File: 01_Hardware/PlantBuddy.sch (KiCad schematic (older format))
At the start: 41 parts, among them J1 SWD+DBG, J2 Conn_I2C_SDA, J3 Conn_I2C_SCL, Q1 AO3401, Q2 AO3400A, U1 OPT3001, U2 nRF52810-QCxx, U3 LMC555xM, U6 SHTC3, Y1 32MHz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

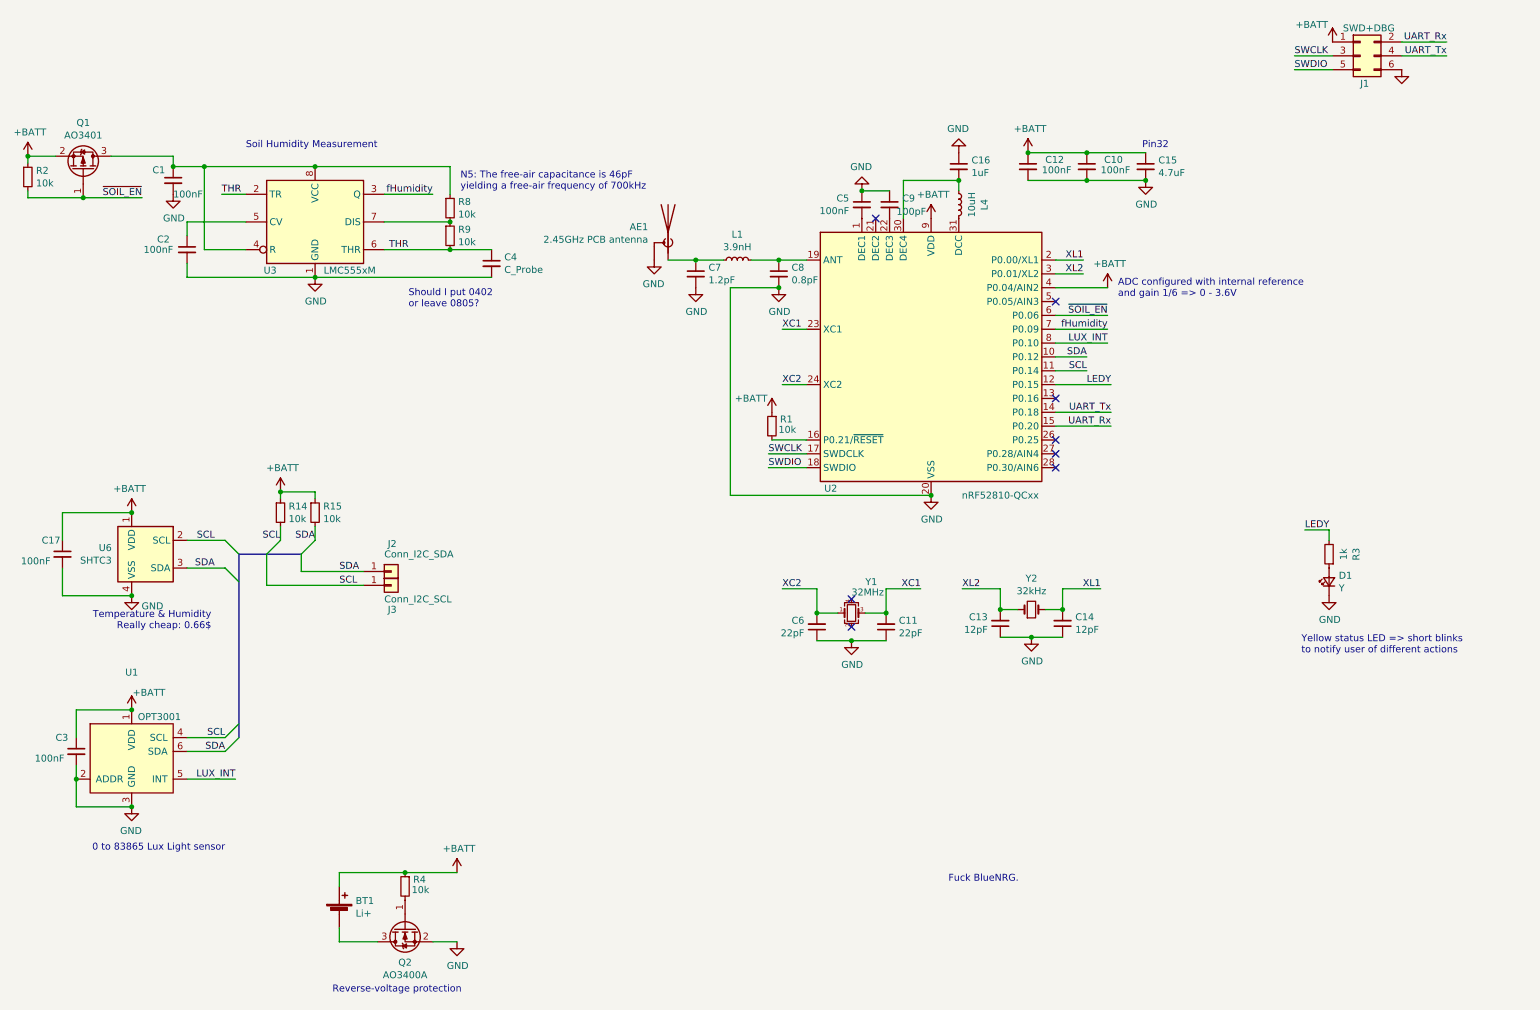
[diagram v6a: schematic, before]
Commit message: PlantBuddy Revision 3. Switched to nRF52832
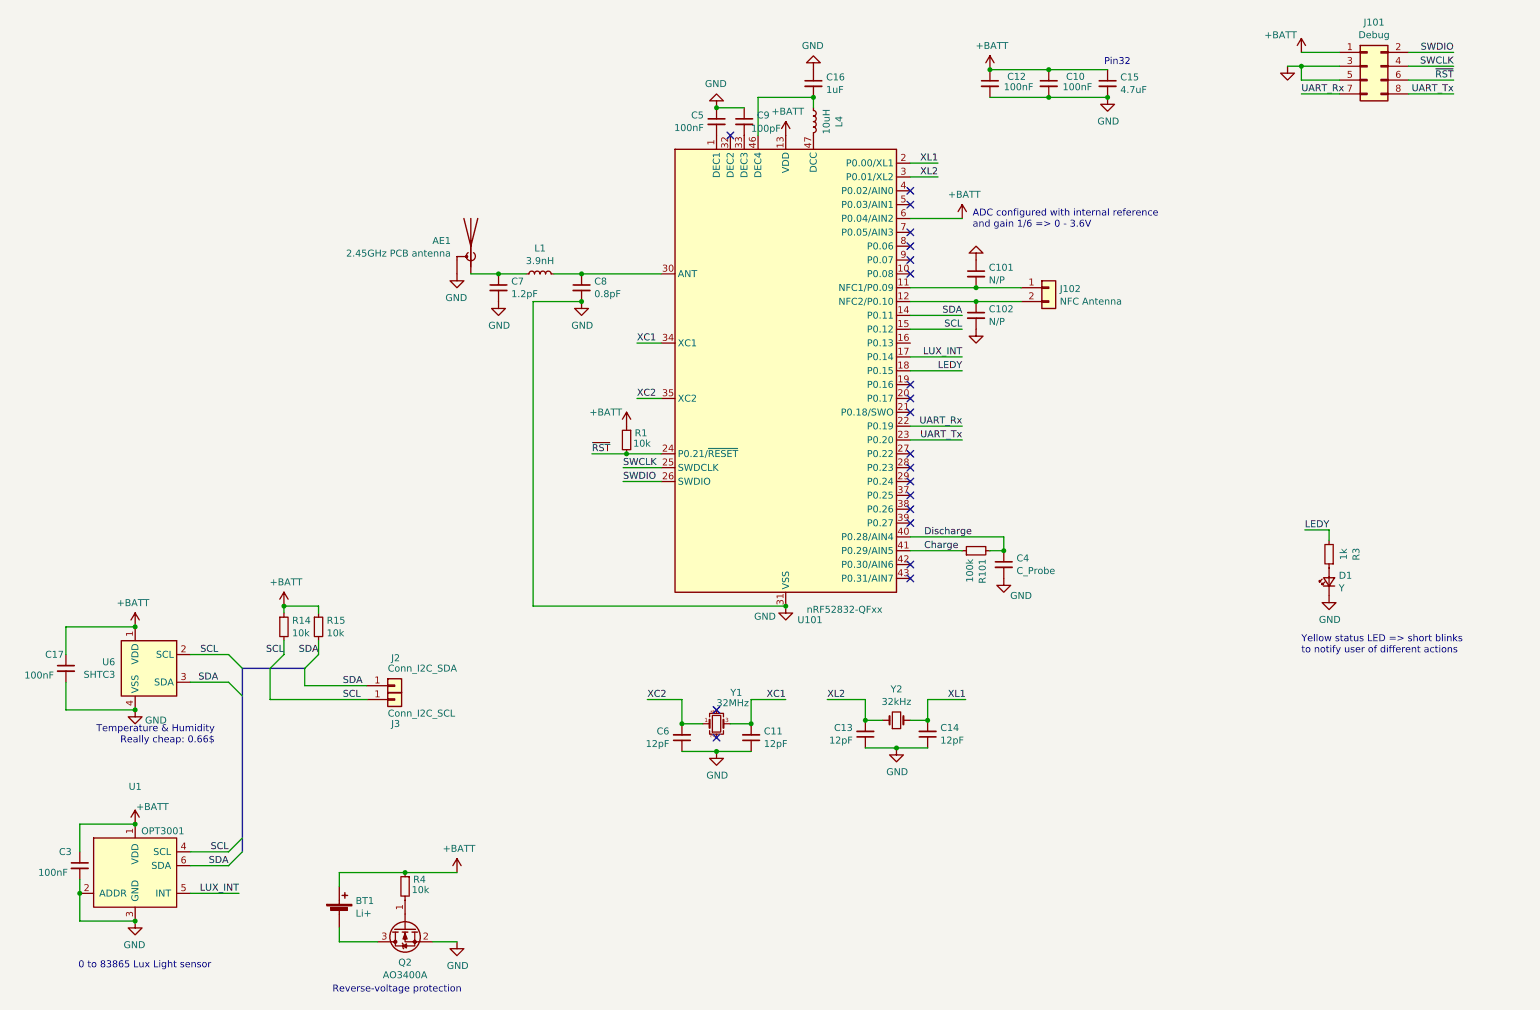
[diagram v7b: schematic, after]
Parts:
- removed C1, C2: 100nF, Capacitor_SMD:C_0402_1005Metric, symbol PlantBuddy-rescue:C_Small-Device
- removed J1: SWD+DBG, Connector_PinHeader_2.54mm:PinHeader_2x03_P2.54mm_Vertical, symbol Connector_Generic:Conn_02x03_Odd_Even
- removed Q1: AO3401, Package_TO_SOT_SMD:SOT-23, symbol PlantBuddy-rescue:AO3401A-Transistor_FET
- removed R2, R8, R9: 10k, Resistor_SMD:R_0402_1005Metric, symbol PlantBuddy-rescue:R_Small-Device
- removed U2: nRF52810-QCxx, Package_DFN_QFN:QFN-32-1EP_5x5mm_P0.5mm_EP3.6x3.6mm_ThermalVias, symbol PlantBuddy-rescue:nRF52810-QCxx-MCU_Nordic
- removed U3: LMC555xM, Package_SO:SOIC-8_3.9x4.9mm_P1.27mm, symbol PlantBuddy-rescue:LMC555xM-Timer
- added C101, C102: N/P, Capacitor_SMD:C_0402_1005Metric, symbol PlantBuddy-rescue:C_Small-Device
- added J101: Debug, PlantBuddy:PinHeader_2x04_P1.27mm_Vertical, symbol Connector_Generic:Conn_02x04_Odd_Even
- added J102: NFC Antenna, Connector_PinHeader_2.54mm:PinHeader_1x02_P2.54mm_Vertical, symbol Connector_Generic:Conn_01x02
- added R101: 100k, Resistor_SMD:R_0402_1005Metric, symbol Device:R_Small
- added U101: nRF52832-QFxx, Package_DFN_QFN:QFN-48-1EP_6x6mm_P0.4mm_EP4.6x4.6mm_ThermalVias, symbol MCU_Nordic:nRF52832-QFxx
- C11, C6: value 22pF -> 12pF
- C8: LCSC C326068 -> C285068
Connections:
- net +BATT: now also J101.1 (Pin_1), U101.13 (VDD), U101.36 (VDD), U101.48 (VDD), U101.6 (P0.04/AIN2)
- net GND: now also C101.1, C102.2, J101.3 (Pin_3), J101.5 (Pin_5), U101.31 (VSS), U101.45 (VSS), U101.49 (VSS)
- net LEDY: now also U101.18 (P0.15)
- net LUX_INT: now also U101.17 (P0.14)
- net SCL: now also U101.15 (P0.12)
- net SDA: now also U101.14 (P0.11)
- net SWCLK: now also J101.4 (Pin_4), U101.25 (SWDCLK)
- net SWDIO: now also J101.2 (Pin_2), U101.26 (SWDIO)
- net UART_Rx: now also J101.7 (Pin_7), U101.22 (P0.19)
- net UART_Tx: now also J101.8 (Pin_8), U101.23 (P0.20)
- net XC1: now also U101.34 (XC1)
- net XC2: now also U101.35 (XC2)
- net XL1: now also U101.2 (P0.00/XL1)
- net XL2: now also U101.3 (P0.01/XL2)
- net at C16.2, L4.1: now also U101.46 (DEC4)
- net at L4.2: now also U101.47 (DCC)
- net at C5.2: now also U101.1 (DEC1)
- net ~RST: now reaches R1.2
- net ~RST: now also J101.6 (Pin_6), U101.24 (P0.21/~RESET)
- net at C8.1, L1.2: now also U101.30 (ANT)
- net at C9.2: now also U101.33 (DEC3)
- net THR renamed Discharge
- net Discharge: now also R101.2, U101.40 (P0.28/AIN4)
- new net: C101.2, J102.1 (Pin_1), U101.11 (NFC1/P0.09)
- new net: C102.1, J102.2 (Pin_2), U101.12 (NFC2/P0.10)
- new net Charge: R101.1, U101.41 (P0.29/AIN5)
- no-connect marks 8 -> 20
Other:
- note removed: "Fuck BlueNRG."
- note removed: "N5: The free-air capacitance is 46pF\nyielding a free-air frequency of 700kHz"
- note removed: "Should I put 0402\nor leave 0805?"
- note removed: "Soil Humidity Measurement"
- moved on the sheet: AE1, C10, C11, C12, C13, C14, C15, C16, C17, C3, C4, C5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
